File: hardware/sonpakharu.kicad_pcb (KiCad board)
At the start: 2 copper layers, 51.3 x 71.1 mm, 63 parts, among them IC1 ESP32-S3-WROOM-1U-N4, J1 ADC4, J10 EXT2, J11 EXT3, J12 BATT, J13 EXT7, J14 PWR, J15 EXT8, J16 FTDI, J17 485, J2 ADC3, J3 ADC2, J4 ADC1, J5 EXT4, J6 I2C, J7 EXT5, J8 EXT1, J9 EXT6, Q1 DMG3415U, Q2 S8050, Q3 S8050, Q4 S8050, SW1 Boot, SW2 Reset, U1 AP2112K-3.3TRG1, U2 MCP73831-2-OT, U3 ADS1115IDGSR, U4 MAX485E

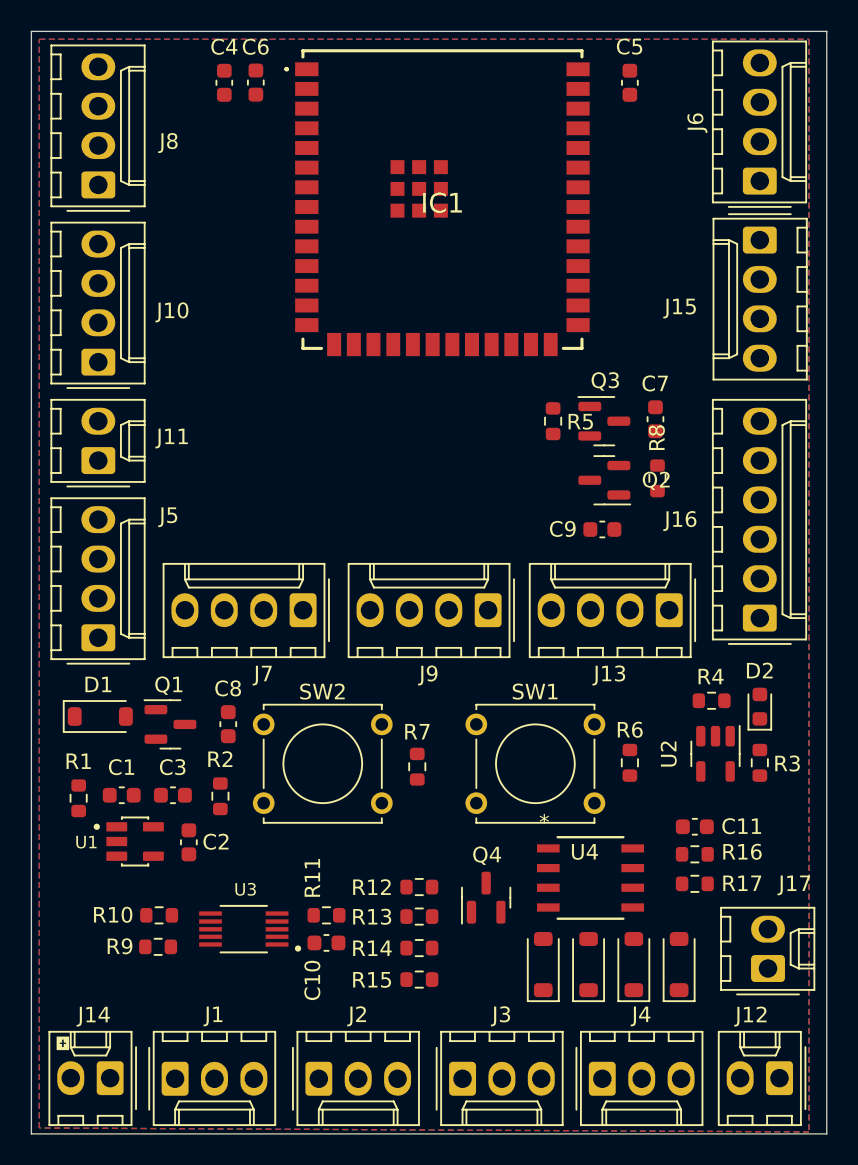
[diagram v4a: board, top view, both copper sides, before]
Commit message: all routing done, no errors, 3 minor warnings
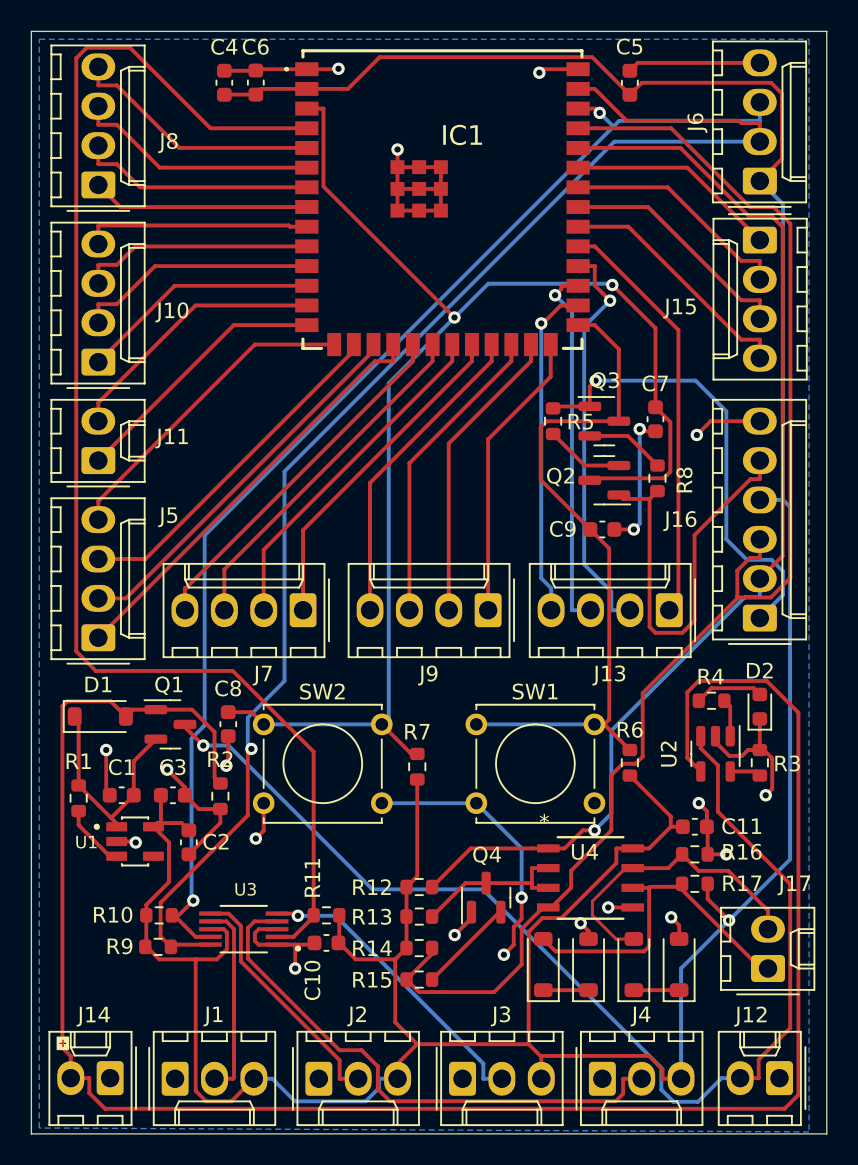
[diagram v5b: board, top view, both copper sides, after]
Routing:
- net +3V3: track 0.00 -> 227.6 mm, vias 0 -> 1
- net VBUS: track 0.00 -> 125.9 mm
- net GND: track 0.00 -> 110.0 mm, vias 0 -> 21
- net /SCL: track 0.00 -> 90.4 mm, vias 0 -> 1
- net /EN: track 0.00 -> 89.7 mm, vias 0 -> 2
- net /TX: track 0.00 -> 89.2 mm
- net /IO4: track 0.00 -> 87.1 mm
- net /SDA: track 0.00 -> 79.4 mm, vias 0 -> 2
- net +BATT: track 0.00 -> 74.0 mm, vias 0 -> 1
- net /RX: track 0.00 -> 71.8 mm, vias 0 -> 1
- net /IO0: track 0.00 -> 44.8 mm
- net /A0: track 0.00 -> 35.3 mm
- net /DTR: track 0.00 -> 29.9 mm, vias 0 -> 1
- net /GP14: track 0.00 -> 27.5 mm
- net /GP26: track 0.00 -> 27.0 mm
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- removed copper zone on F.Cu, net GND

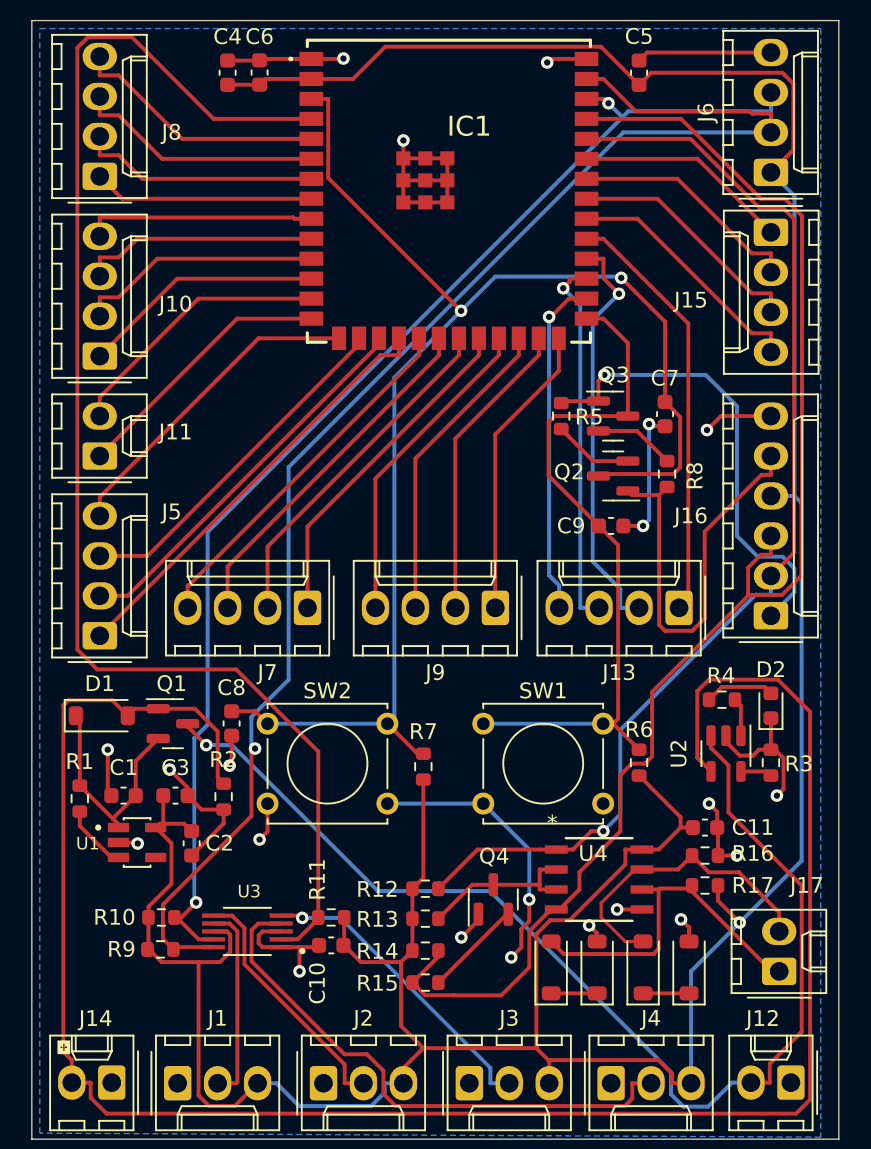
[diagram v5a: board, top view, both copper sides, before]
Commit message: corrected placement
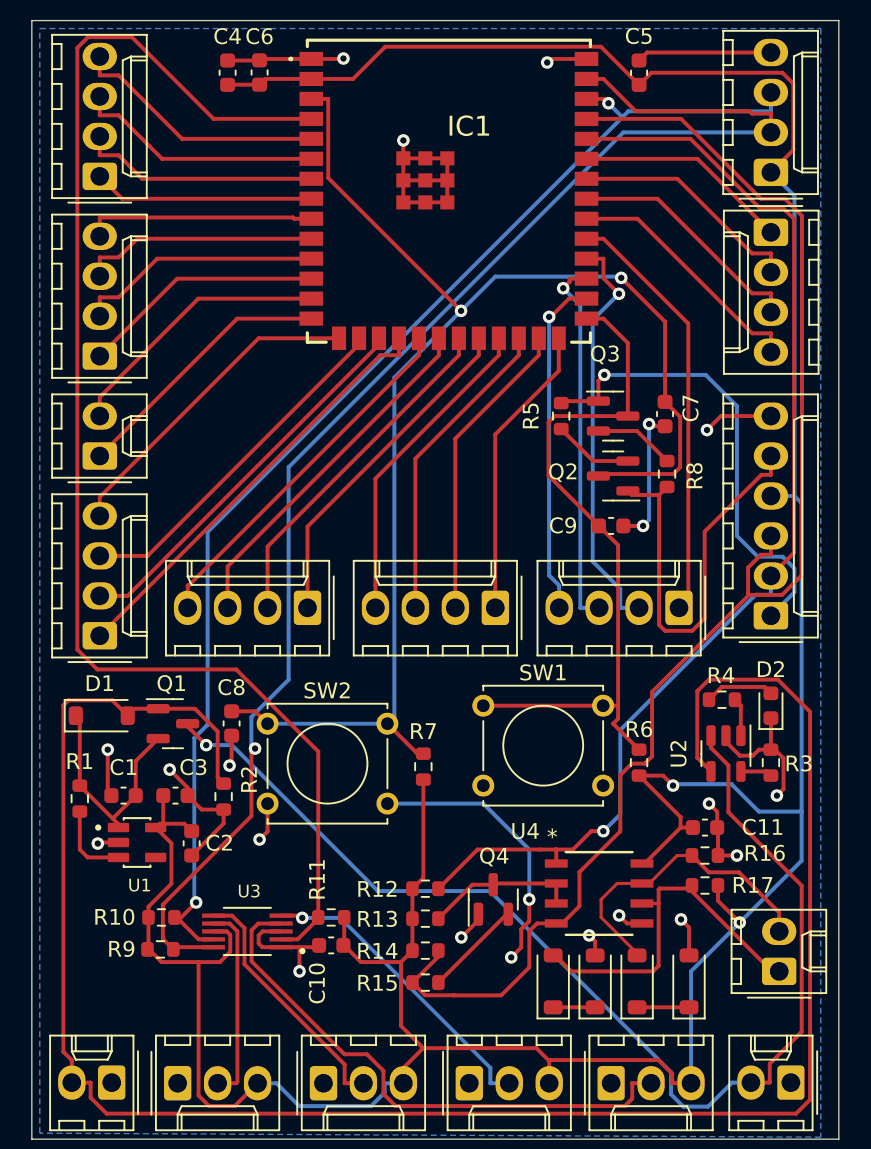
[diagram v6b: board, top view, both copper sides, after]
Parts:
- removed kibuzzard-6592A79E: G***, kibuzzard-6592A79E
- moved SW1 1.14 mm to (134.6, 81.2)
- moved D5 0.97 mm to (144.4, 98.7)
- moved D3 0.90 mm to (139.1, 98.7)
- moved D4 0.90 mm to (141.7, 98.7)
- moved U4 0.89 mm to (142.0, 93.1)
- moved D6 0.89 mm to (147.7, 98.7)
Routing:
- net +3V3: track 227.6 -> 222.6 mm, vias 1 -> 2
- net GND: track 110.0 -> 111.2 mm
- net Net-(Q4-C): track 10.7 -> 9.62 mm
- net /D+: track 22.3 -> 23.3 mm
- net /RX: track 71.8 -> 72.7 mm
- net Net-(U1-EN): track 4.20 -> 5.08 mm
- net /TX: track 89.2 -> 89.8 mm

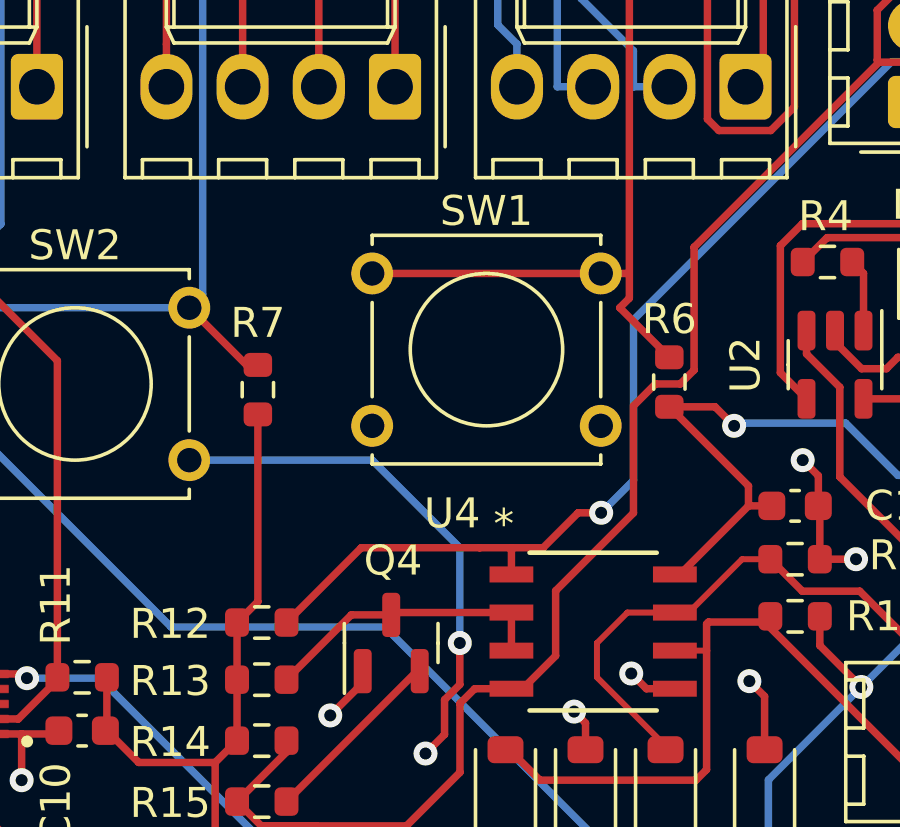
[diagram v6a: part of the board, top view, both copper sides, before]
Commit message: track correction and tactile switch footprint pending
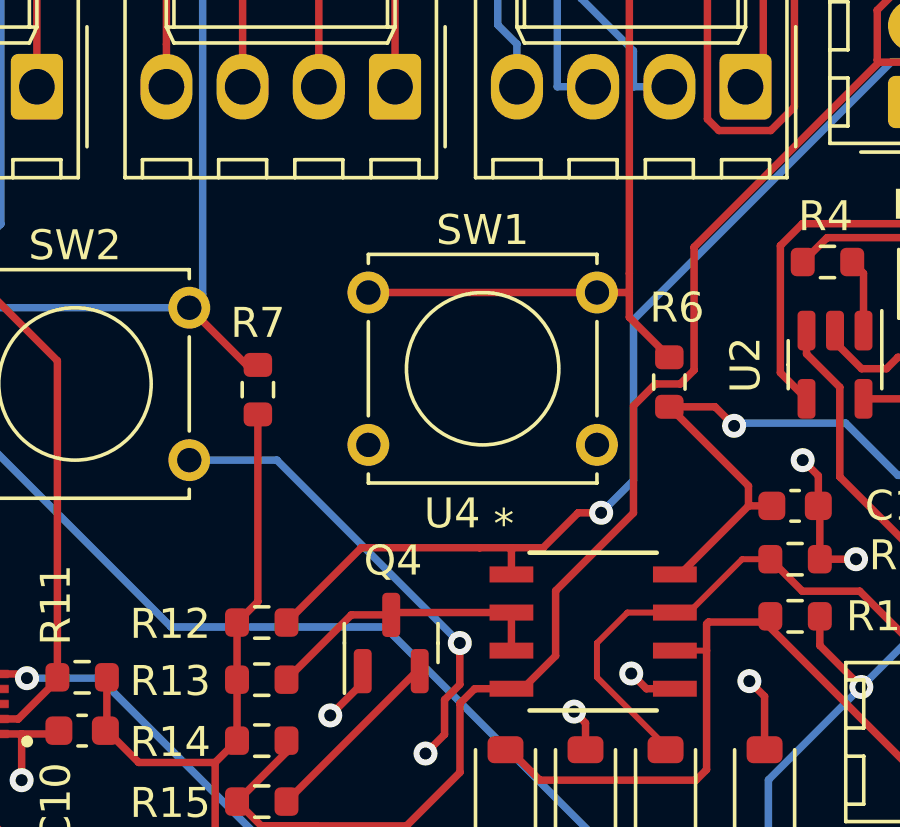
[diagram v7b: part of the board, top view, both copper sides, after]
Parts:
- moved SW1 0.65 mm to (134.5, 81.8)
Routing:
- net GND: track 111.2 -> 109.4 mm
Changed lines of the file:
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@@
     (property "ki_keywords" "R res resistor")
     (attr smd)
-    (fp_text reference "R6" (at 2.095 0) (layer "F.SilkS")
+    (fp_text reference "R6" (at 2.477 0.254) (layer "F.SilkS")
         (effects (font (size 1 1) (thickness 0.15)))
     )
@@
   )
   (footprint "Button_Switch_THT:SW_Tactile_Straight_KSA0Axx1LFTR" (layer "F.Cu")
-    (at 134.62 81.153)
+    (at 134.493 81.788)
     (descr "SW PUSH SMALL http://www.ckswitches.com/media/1457/ksa_ksl.pdf")
     (tags "SW PUSH SMALL Tactile C&K")
@@
   (via (at 147.193 94.742) (size 0.8) (drill 0.4) (layers "F.Cu" "B.Cu") (net 2))
   (via (at 143.256 94.488) (size 0.8) (drill 0.4) (layers "F.Cu" "B.Cu") (net 2))
-  (segment (start 137.541 90.297) (end 137.541 93.472) (width 0.25) (layer "B.Cu") (net 2))
-  (segment (start 134.62 87.376) (end 128.524 87.376) (width 0.25) (layer "B.Cu") (net 2))
-  (segment (start 134.62 87.376) (end 137.541 90.297) (width 0.25) (layer "B.Cu") (net 2))
   (segment (start 145.161 69.342) (end 145.161 63.246) (width 0.25) (layer "B.Cu") (net 2))
   (segment (start 144.78 69.723) (end 145.161 69.342) (width 0.25) (layer "B.Cu") (net 2))
+  (segment (start 131.445 87.376) (end 137.541 93.472) (width 0.25) (layer "B.Cu") (net 2))
+  (segment (start 128.524 87.376) (end 131.445 87.376) (width 0.25) (layer "B.Cu") (net 2))
   (segment (start 113.3005 96.647) (end 113.332 96.6155) (width 0.25) (layer "F.Cu") (net 3))
   (segment (start 145.7559 103.6824) (end 138.8627 103.6824) (width 0.25) (layer "F.Cu") (net 3))
@@
   (segment (start 143.8125 58.0936) (end 143.8125 62.738) (width 0.25) (layer "F.Cu") (net 5))
   (segment (start 138.7692 63.1348) (end 139.166 62.738) (width 0.25) (layer "F.Cu") (net 5))
-  (segment (start 143.1925 81.9775) (end 143.1925 81.153) (width 0.25) (layer "F.Cu") (net 5))
-  (segment (start 142.874 82.296) (end 143.1925 81.9775) (width 0.25) (layer "F.Cu") (net 5))
+  (segment (start 143.1925 81.788) (end 143.1925 81.153) (width 0.25) (layer "F.Cu") (net 5))
   (segment (start 143.1925 70.9425) (end 141.973 69.723) (width 0.25) (layer "F.Cu") (net 5))
   (segment (start 142.2609 56.542) (end 143.8125 58.0936) (width 0.25) (layer "F.Cu") (net 5))
-  (segment (start 142.24 81.153) (end 134.62 81.153) (width 0.25) (layer "F.Cu") (net 5))
   (segment (start 143.1925 81.153) (end 143.1925 70.9425) (width 0.25) (layer "F.Cu") (net 5))
+  (segment (start 142.113 81.788) (end 134.493 81.788) (width 0.25) (layer "F.Cu") (net 5))
   (segment (start 138.7692 66.5192) (end 138.7692 63.1348) (width 0.25) (layer "F.Cu") (net 5))
-  (segment (start 142.874 82.296) (end 144.526 83.948) (width 0.25) (layer "F.Cu") (net 5))
-  (segment (start 142.24 81.153) (end 143.1925 81.153) (width 0.25) (layer "F.Cu") (net 5))
+  (segment (start 143.1925 82.6145) (end 143.1925 81.788) (width 0.25) (layer "F.Cu") (net 5))
   (segment (start 141.973 69.723) (end 138.7692 66.5192) (width 0.25) (layer "F.Cu") (net 5))
+  (segment (start 142.113 81.788) (end 143.1925 81.788) (width 0.25) (layer "F.Cu") (net 5))
   (segment (start 139.166 62.738) (end 143.8125 62.738) (width 0.25) (layer "F.Cu") (net 5))
+  (segment (start 144.526 83.948) (end 143.1925 82.6145) (width 0.25) (layer "F.Cu") (net 5))
   (segment (start 111.0354 80.8094) (end 108.2374 80.8094) (width 0.25) (layer "F.Cu") (net 6))
   (segment (start 107.9211 103.1572) (end 108.458 103.6941) (width 0.25) (layer "F.Cu") (net 6))

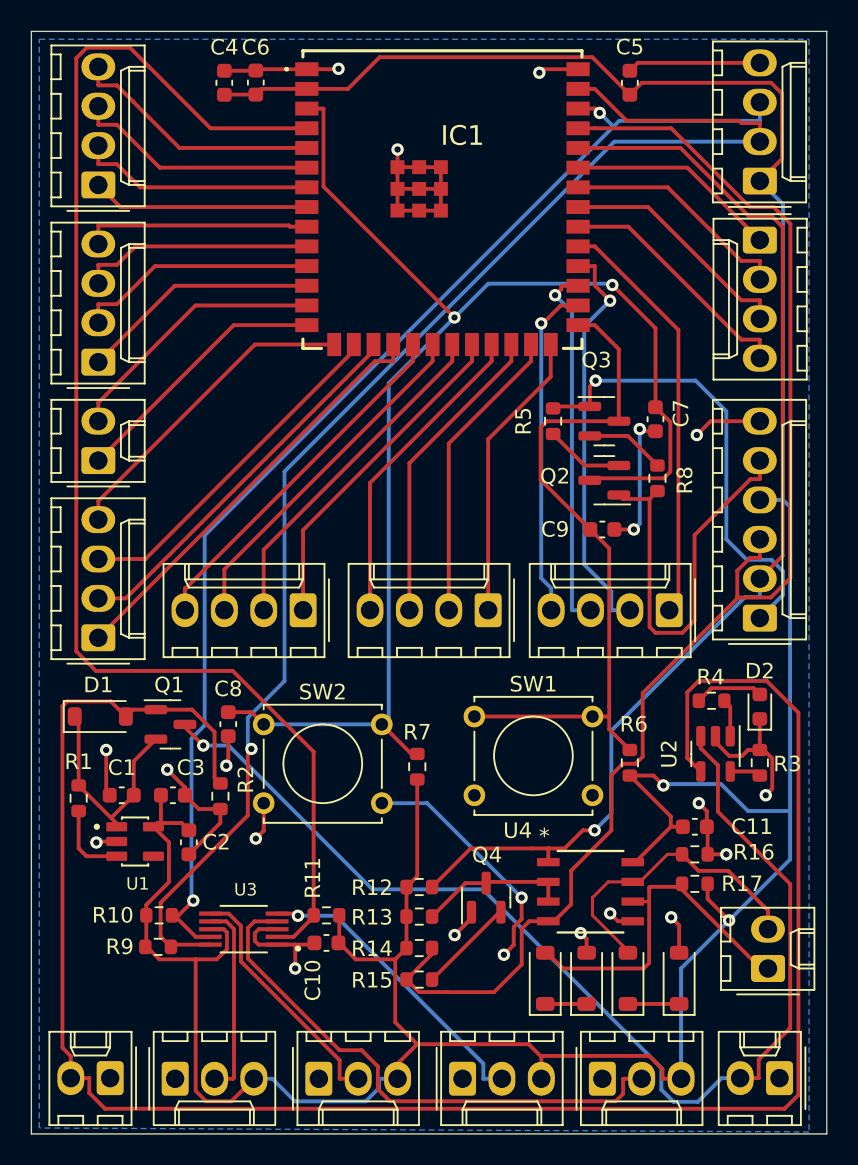
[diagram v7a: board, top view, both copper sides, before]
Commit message: almost all tracks corrected, added tactile smd
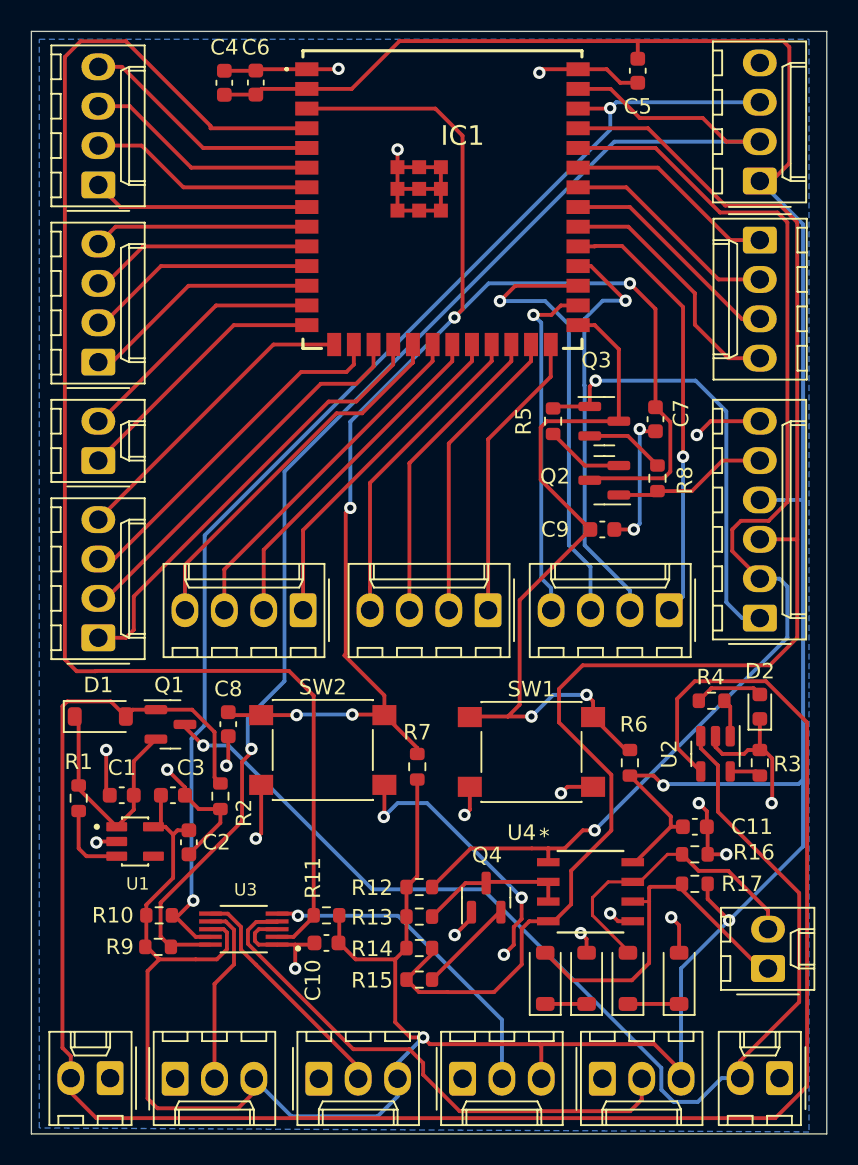
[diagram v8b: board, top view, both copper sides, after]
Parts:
- SW1, SW2: footprint Button_Switch_THT:SW_Tactile_Straight_KSA0Axx1LFTR -> Button_Switch_SMD:SW_Push_1P1T_NO_6x6mm_H9.5mm
- moved SW1 4.33 mm to (138.2, 84.1)
- moved SW2 4.15 mm to (124.7, 83.9)
- moved C5 0.93 mm to (145.0, 40.1), turned to -90 degrees
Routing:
- net /RTS: track 26.9 -> 10.0 mm
- net +3V3: track 222.6 -> 235.2 mm, vias 2 -> 3
- net /EN: track 89.7 -> 96.8 mm, vias 2 -> 5
- net /TX: track 89.8 -> 96.3 mm
- net /GP24: track 23.8 -> 29.5 mm
- net /RX: track 72.7 -> 77.5 mm
- net /IO4: track 87.1 -> 91.5 mm
- net GND: track 109.4 -> 113.1 mm, vias 21 -> 24
- net /IO0: track 45.0 -> 48.0 mm, vias 0 -> 2
- net /A1: track 19.5 -> 21.1 mm
- net VBUS: track 125.9 -> 127.5 mm
- net /DTR: track 29.9 -> 28.4 mm
- net /GP14: track 27.5 -> 28.9 mm
- net /GP26: track 27.0 -> 28.3 mm, vias 0 -> 1
- net /GP23: track 21.6 -> 22.7 mm
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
